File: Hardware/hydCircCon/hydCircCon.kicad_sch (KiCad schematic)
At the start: 76 parts, among them J1 USB_B_Micro, J10 Conn_01x03, J16 Conn_01x02, J17 Conn_01x02, J2 Conn_01x03, J5 Conn_01x02, J6 Conn_01x03, J7 Conn_01x03, J8 Conn_01x02, J9 Conn_01x02, U1 W25Q16JVUXIQ, U2 RP2040, U3 MCP6001R, U4 AP63357Q, U8 AP2127K-ADJ, Y1 12Mhz

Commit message: wip
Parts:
- R1, R2: value 20R -> 10R
- R10, R11: value 1k -> 100R
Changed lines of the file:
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@@
       (effects (font (size 1.27 1.27)) (justify right))
     )
-    (property "Value" "1k" (id 1) (at 137.16 186.69 90)
+    (property "Value" "100R" (id 1) (at 138.43 186.69 90)
       (effects (font (size 1.27 1.27)) (justify right))
     )
@@
       (effects (font (size 1.27 1.27)) (justify right))
     )
-    (property "Value" "20R" (id 1) (at 36.83 66.04 90)
+    (property "Value" "10R" (id 1) (at 36.83 66.04 90)
       (effects (font (size 1.27 1.27)) (justify right))
     )
@@
       (effects (font (size 1.27 1.27)) (justify right))
     )
-    (property "Value" "20R" (id 1) (at 36.83 60.96 90)
+    (property "Value" "10R" (id 1) (at 36.83 60.96 90)
       (effects (font (size 1.27 1.27)) (justify right))
     )
@@
       (effects (font (size 1.27 1.27)) (justify right))
     )
-    (property "Value" "1k" (id 1) (at 137.16 176.53 90)
+    (property "Value" "100R" (id 1) (at 138.43 176.53 90)
       (effects (font (size 1.27 1.27)) (justify right))
     )
@@
     )
     (path "/77f95415-68a4-4d83-8ab1-52173e95cff3"
-      (reference "R1") (unit 1) (value "20R") (footprint "Resistor_SMD:R_0603_1608Metric")
+      (reference "R1") (unit 1) (value "10R") (footprint "Resistor_SMD:R_0603_1608Metric")
     )
     (path "/64515f6d-43e0-4377-af00-dd3dbbe6ee6f"
-      (reference "R2") (unit 1) (value "20R") (footprint "Resistor_SMD:R_0603_1608Metric")
+      (reference "R2") (unit 1) (value "10R") (footprint "Resistor_SMD:R_0603_1608Metric")
     )
     (path "/3ae19f08-4786-40ec-9bba-e1a5ab76fd3b"
@@
     )
     (path "/dd27579f-db8a-476a-9863-077446cad09a/7941c371-a191-4ebd-a3e1-826dc657baf4"
-      (reference "R6") (unit 1) (value "1k") (footprint "Resistor_SMD:R_0603_1608Metric")
+      (reference "R6") (unit 1) (value "100R") (footprint "Resistor_SMD:R_0603_1608Metric")
     )
     (path "/dd27579f-db8a-476a-9863-077446cad09a/1dd6b72c-7bbc-4e6e-b66b-d4b818cc002e"
-      (reference "R7") (unit 1) (value "1k") (footprint "Resistor_SMD:R_0603_1608Metric")
+      (reference "R7") (unit 1) (value "100R") (footprint "Resistor_SMD:R_0603_1608Metric")
     )
     (path "/0983039d-4d5b-4ff1-bc83-1276a8f25a31"
@@
     )
     (path "/e402d2f0-1e49-43c8-9995-fcc60d361f56"
-      (reference "R10") (unit 1) (value "1k") (footprint "Resistor_SMD:R_0603_1608Metric")
+      (reference "R10") (unit 1) (value "100R") (footprint "Resistor_SMD:R_0603_1608Metric")
     )
     (path "/24931fe9-cc00-4037-adda-906d31e58785"
-      (reference "R11") (unit 1) (value "1k") (footprint "Resistor_SMD:R_0603_1608Metric")
+      (reference "R11") (unit 1) (value "100R") (footprint "Resistor_SMD:R_0603_1608Metric")
     )
     (path "/9faea613-0b2d-4cc6-9eaf-fec0075192b0"
@@
     )
     (path "/dd27579f-db8a-476a-9863-077446cad09a/e08e5d39-9d65-4a3b-9a84-7e0ecdc406b5"
-      (reference "R27") (unit 1) (value "50R") (footprint "Resistor_SMD:R_0603_1608Metric")
+      (reference "R27") (unit 1) (value "51R") (footprint "Resistor_SMD:R_0603_1608Metric")
     )
     (path "/dd27579f-db8a-476a-9863-077446cad09a/8a154e9b-c857-44a8-b1c8-79c28c7deecc"
-      (reference "R28") (unit 1) (value "50R") (footprint "Resistor_SMD:R_0603_1608Metric")
+      (reference "R28") (unit 1) (value "51R") (footprint "Resistor_SMD:R_0603_1608Metric")
     )
     (path "/dd27579f-db8a-476a-9863-077446cad09a/298d15ad-fc72-4f92-b870-a116236bd2d4"

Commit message: wip
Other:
- note added: "Notiz für V2.0: -) Spannunsgmessung 24V sinvvol"
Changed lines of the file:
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@@
+    (effects (font (size 1.27 1.27)) (justify left bottom))
+  )
+  (text "Notiz für V2.0:\n-) Spannunsgmessung 24V sinvvol" (at 92.71 152.4 0)
     (effects (font (size 1.27 1.27)) (justify left bottom))
   )

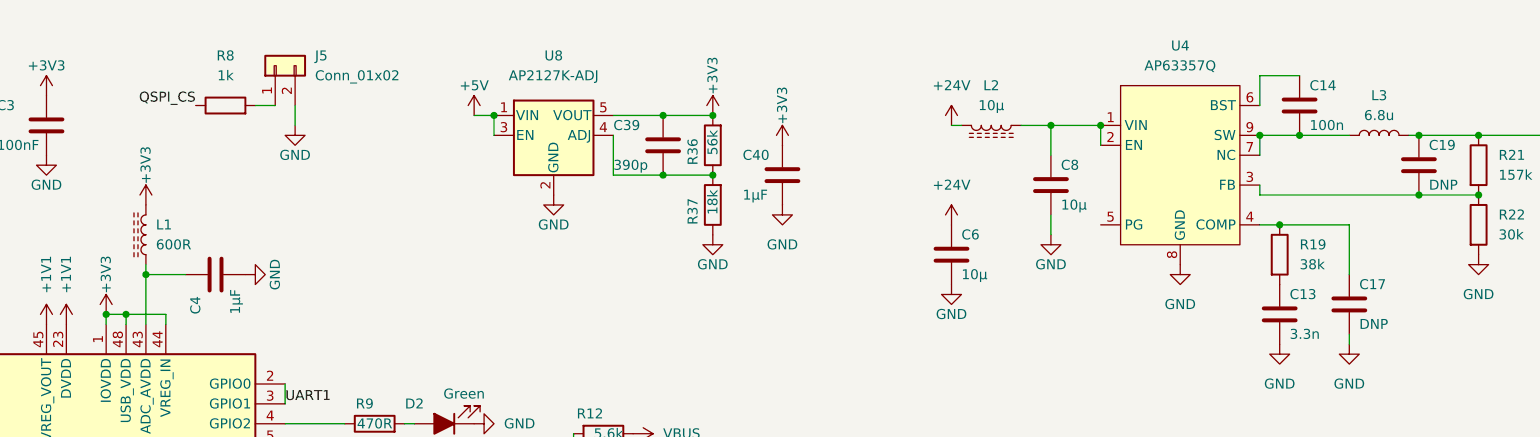
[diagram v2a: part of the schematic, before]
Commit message: modified motor output
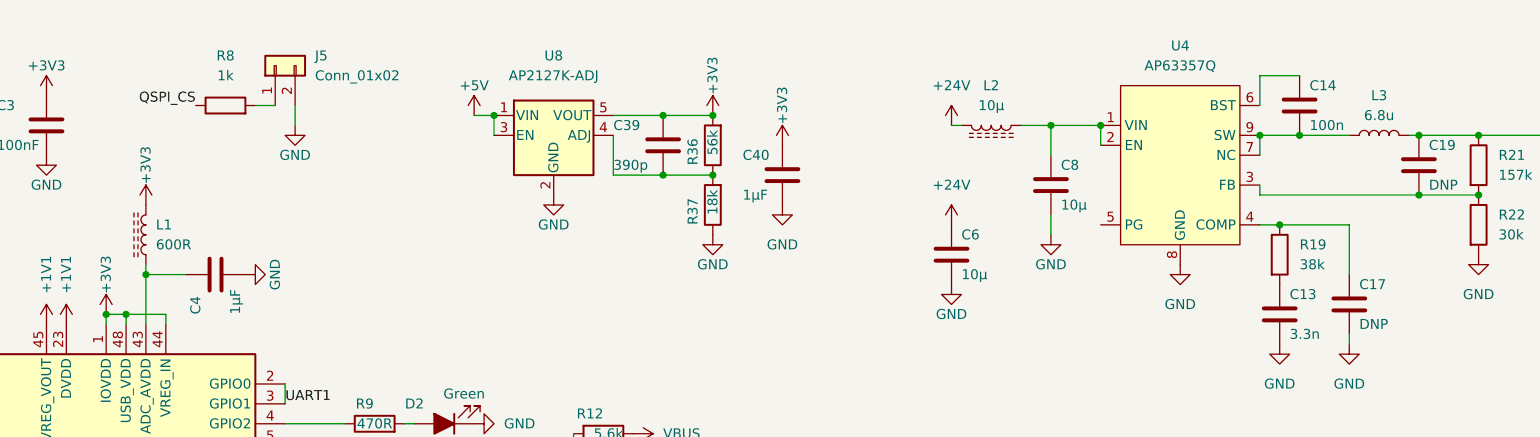
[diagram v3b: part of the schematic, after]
